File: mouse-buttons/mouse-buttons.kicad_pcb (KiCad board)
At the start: 2 copper layers, 58 x 15.5 mm, 9 parts

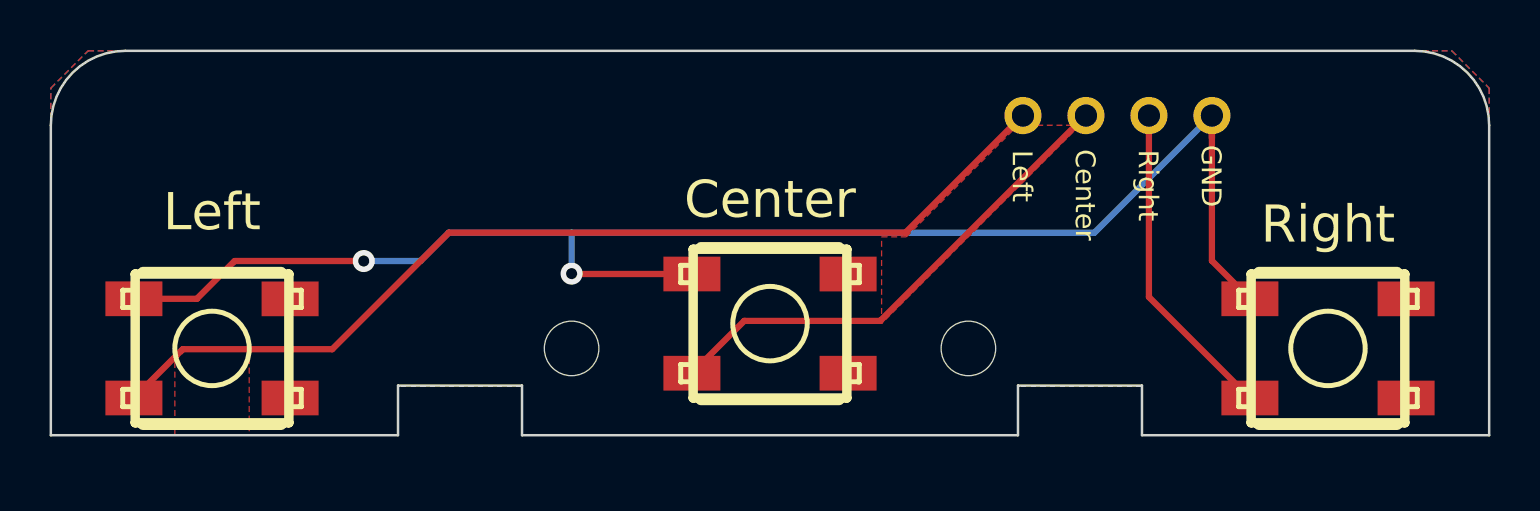
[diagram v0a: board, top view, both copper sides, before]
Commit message: Revised mouse buttons PCB and added precise measurements for mouse buttons and TrackPoint holes.
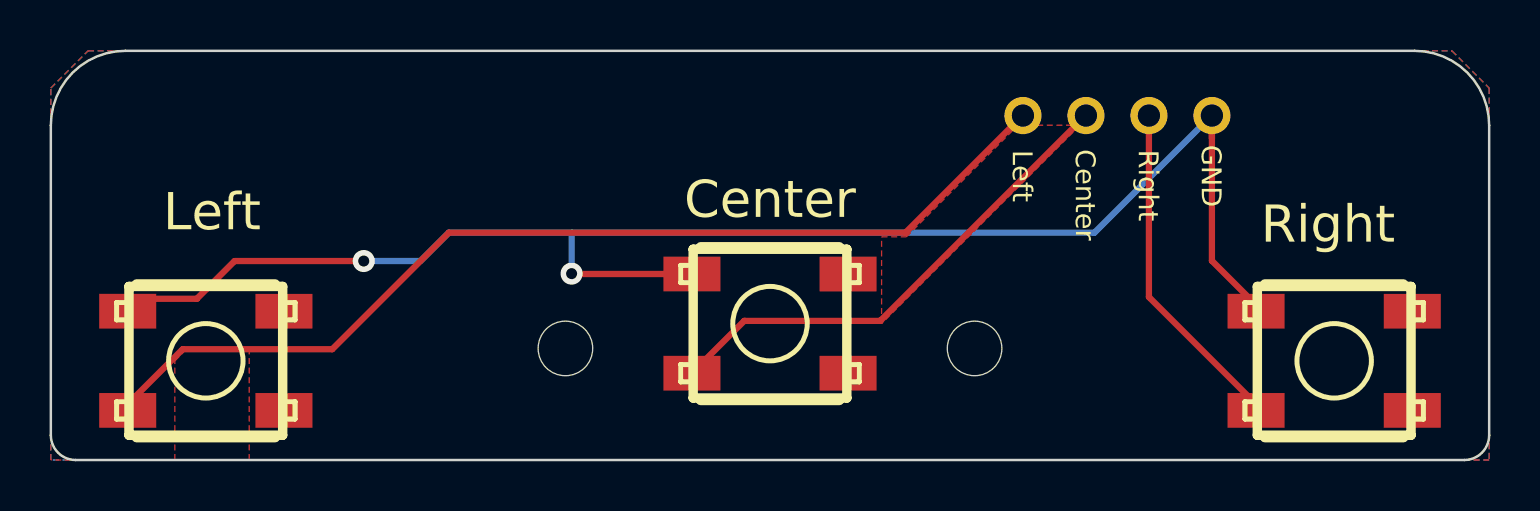
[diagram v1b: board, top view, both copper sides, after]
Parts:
- moved SL0 0.56 mm to (239.2, 129.5)
- moved SR0 0.56 mm to (284.8, 129.5)
- moved ? 0.25 mm to (270.2, 129.0)
- moved ? 0.25 mm to (253.8, 129.0)
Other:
- board size 58 x 15.5 mm -> 58 x 16.5 mm
